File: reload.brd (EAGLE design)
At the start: 49.2 x 30.5 mm, 19 parts, among them IC1 LM358, Q1 BTS117, U1 TL431

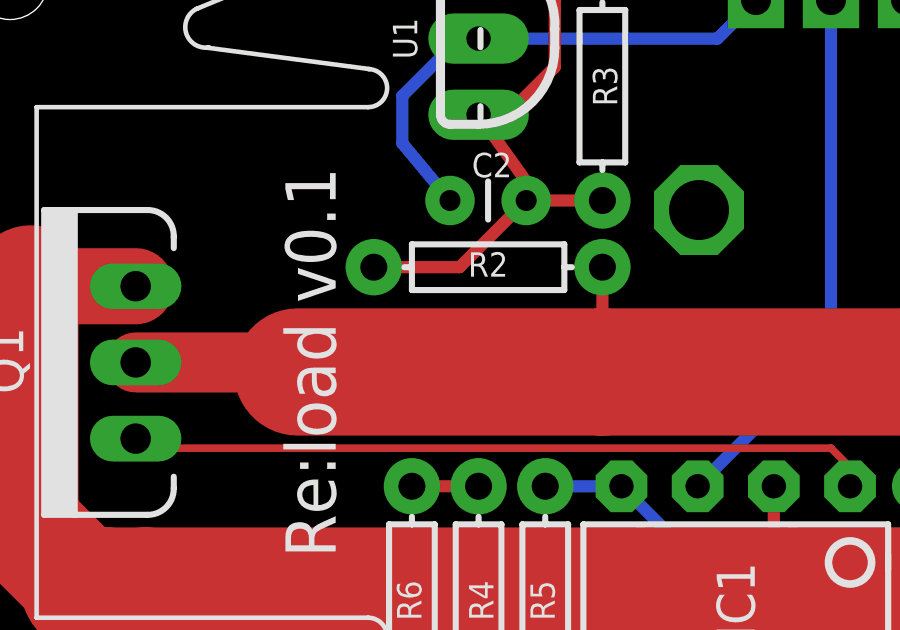
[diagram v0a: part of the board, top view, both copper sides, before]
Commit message: Updated schematic, layout tweak.
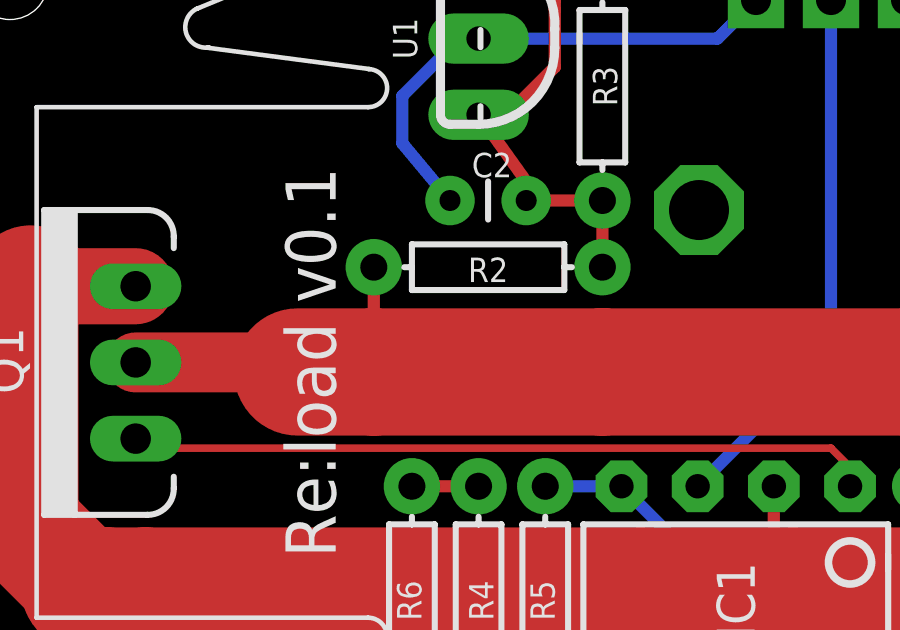
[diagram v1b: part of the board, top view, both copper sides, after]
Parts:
- turned R2 to 180 degrees
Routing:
- net N$5: track 20.4 -> 16.6 mm
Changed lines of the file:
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@@
 <attribute name="NAME" x="14.605" y="26.035" size="0.8128" layer="25" ratio="10" rot="R270" align="bottom-center"/>
 </element>
-<element name="R2" library="SparkFun-Passives" package="AXIAL-0.3" value="787" x="17.78" y="18.415" smashed="yes">
-<attribute name="NAME" x="17.78" y="18.0975" size="0.8128" layer="25" font="vector" align="bottom-center"/>
+<element name="R2" library="SparkFun-Passives" package="AXIAL-0.3" value="787" x="17.78" y="18.415" smashed="yes" rot="R180">
+<attribute name="NAME" x="17.78" y="18.7325" size="0.8128" layer="25" font="vector" rot="R180" align="bottom-center"/>
 </element>
 <element name="C1" library="SparkFun-Passives" package="CAP-PTH-SMALL" value="0.1u" x="32.0675" y="11.1125" smashed="yes">
@@
 <wire x1="40.9575" y1="17.78" x2="45.64" y2="17.78" width="4.2418" layer="1"/>
 <wire x1="45.64" y1="17.78" x2="45.72" y2="17.7" width="4.2418" layer="1"/>
-<wire x1="11.43" y1="14.9225" x2="21.59" y2="14.9225" width="4.2418" layer="1"/>
+<wire x1="11.43" y1="14.9225" x2="13.97" y2="14.9225" width="4.2418" layer="1"/>
+<wire x1="13.97" y1="14.9225" x2="21.59" y2="14.9225" width="4.2418" layer="1"/>
 <wire x1="21.59" y1="14.9225" x2="31.75" y2="14.9225" width="4.2418" layer="1"/>
 <wire x1="31.75" y1="14.9225" x2="36.5125" y2="14.9225" width="4.2418" layer="1"/>
 <wire x1="6.0325" y1="15.24" x2="11.1125" y2="15.24" width="2" layer="1"/>
 <wire x1="11.1125" y1="15.24" x2="11.43" y2="14.9225" width="2" layer="1"/>
-<wire x1="21.59" y1="18.415" x2="21.59" y2="14.9225" width="0.4064" layer="1"/>
 <wire x1="32.0675" y1="11.1125" x2="32.0675" y2="14.605" width="0.4064" layer="1"/>
 <wire x1="32.0675" y1="14.605" x2="31.75" y2="14.9225" width="0.4064" layer="1"/>
@@
 <wire x1="38.1" y1="3.4925" x2="40.9575" y2="6.35" width="0.4064" layer="1"/>
 <wire x1="40.9575" y1="6.35" x2="40.9575" y2="17.78" width="0.4064" layer="1"/>
+<wire x1="13.97" y1="18.415" x2="13.97" y2="14.9225" width="0.4064" layer="1"/>
 </signal>
 <signal name="N$2">
@@
 <wire x1="20.0025" y1="27.305" x2="18.7325" y2="28.575" width="0.4064" layer="1"/>
 <wire x1="18.7325" y1="28.575" x2="17.4625" y2="28.575" width="0.4064" layer="1"/>
-<wire x1="13.97" y1="18.415" x2="16.8275" y2="18.415" width="0.4064" layer="1"/>
-<wire x1="16.8275" y1="18.415" x2="19.05" y2="20.6375" width="0.4064" layer="1"/>
+<wire x1="21.59" y1="18.415" x2="21.59" y2="20.6375" width="0.4064" layer="1"/>
 </signal>
 <signal name="N$6">
